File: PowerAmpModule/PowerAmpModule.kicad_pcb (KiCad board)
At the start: 2 copper layers, 156 x 60 mm, 20 parts, among them J1 Signal, J2 Power, J3 SignalOut, J4 Heater, J5 HeaterOut, J6 PowerOut, J7 Inductor, U1 6V6, U2 6V6

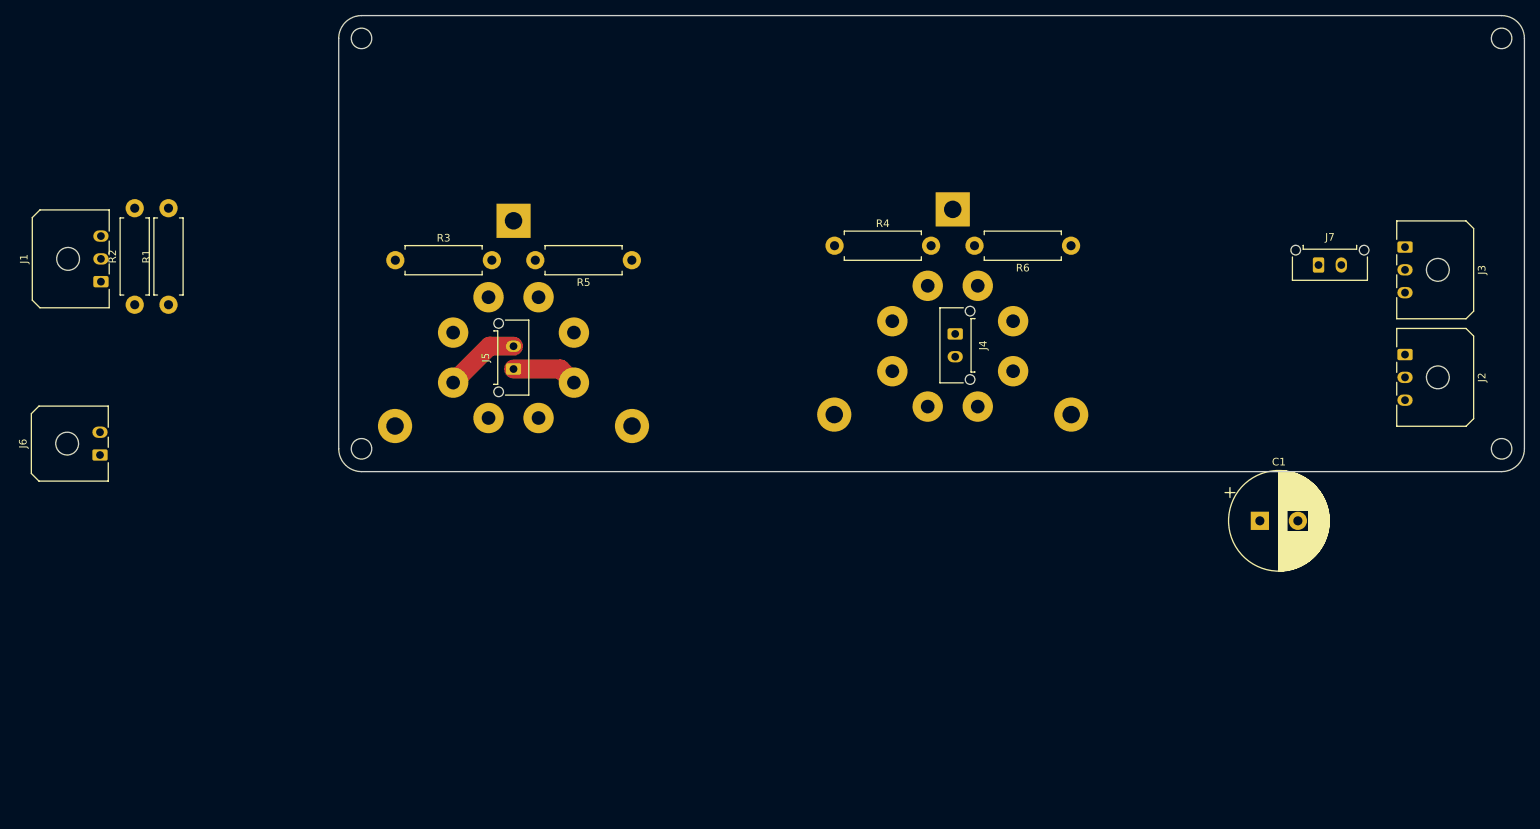
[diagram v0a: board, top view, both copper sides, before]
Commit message: Standardized hole size across all boards
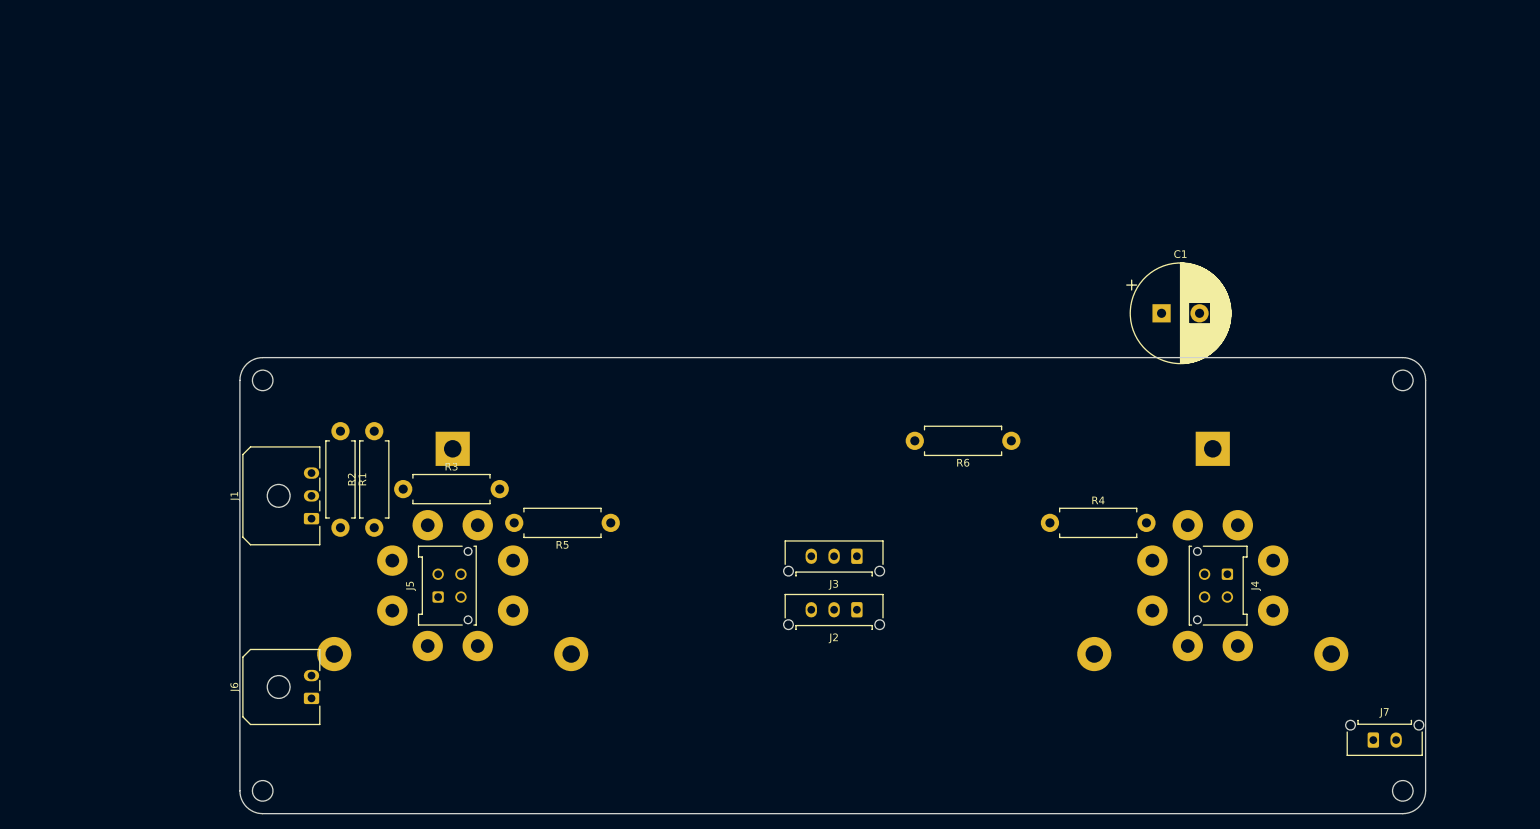
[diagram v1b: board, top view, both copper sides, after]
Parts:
- J1: footprint Connector_Molex:Molex_Micro-Fit_3.0_43650-0300_1x03_P3.00mm_Horizontal -> CustomFootprints:Molex_Micro-Fit_3.0_43650-0300_1x03_P3.00mm_Horizontal
- J2, J3: footprint Connector_Molex:Molex_Micro-Fit_3.0_43650-0300_1x03_P3.00mm_Horizontal -> CustomFootprints:Molex_Micro-Fit_3.0_43650-0315_1x03_P3.00mm_Vertical
- J4, J5: footprint Connector_Molex:Molex_Micro-Fit_3.0_43650-0215_1x02_P3.00mm_Vertical -> CustomFootprints:Molex_Micro-Fit_3.0_43045-0412_2x02_P3.00mm_Vertical
- J6: footprint Connector_Molex:Molex_Micro-Fit_3.0_43650-0200_1x02_P3.00mm_Horizontal -> CustomFootprints:Molex_Micro-Fit_3.0_43650-0200_1x02_P3.00mm_Horizontal
- J7: footprint Connector_Molex:Molex_Micro-Fit_3.0_43650-0215_1x02_P3.00mm_Vertical -> CustomFootprints:Molex_Micro-Fit_3.0_43650-0215_1x02_P3.00mm_Vertical
- moved J3 82.8 mm to (149.6, 101.8), turned to 180 degrees
- moved J2 79.5 mm to (149.6, 108.9), turned to 180 degrees
- moved J7 62.9 mm to (217.6, 126.0)
- moved J4 47.8 mm to (198.4, 104.2)
- moved REF** 46.8 mm to (221.4, 132.7)
- moved REF** 46.8 mm to (71.4, 132.7)
- moved REF** 46.8 mm to (71.4, 78.7)
- moved REF** 46.8 mm to (221.4, 78.7)
- moved U2 46.5 mm to (196.4, 105.7)
- moved R4 46.2 mm to (175.0, 97.4)
- moved R2 43.1 mm to (86.1, 98.1)
- moved J6 42.4 mm to (77.9, 120.5)
- moved J1 41.7 mm to (77.9, 96.9)
- moved R5 34.7 mm to (117.2, 97.4)
- moved J5 31.6 mm to (94.5, 107.2)
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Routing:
- net Net-(J4-Pin_2): track 9.93 -> 0.00 mm
- net Net-(J4-Pin_1): track 8.69 -> 0.00 mm
